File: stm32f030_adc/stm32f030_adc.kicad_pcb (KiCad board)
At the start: 2 copper layers, 41 parts, among them Q1 BC337, U1 STM32F103C6Tx, U2 AMS1117-3.3, X1 USB_B_Micro, Y2 8 MHz

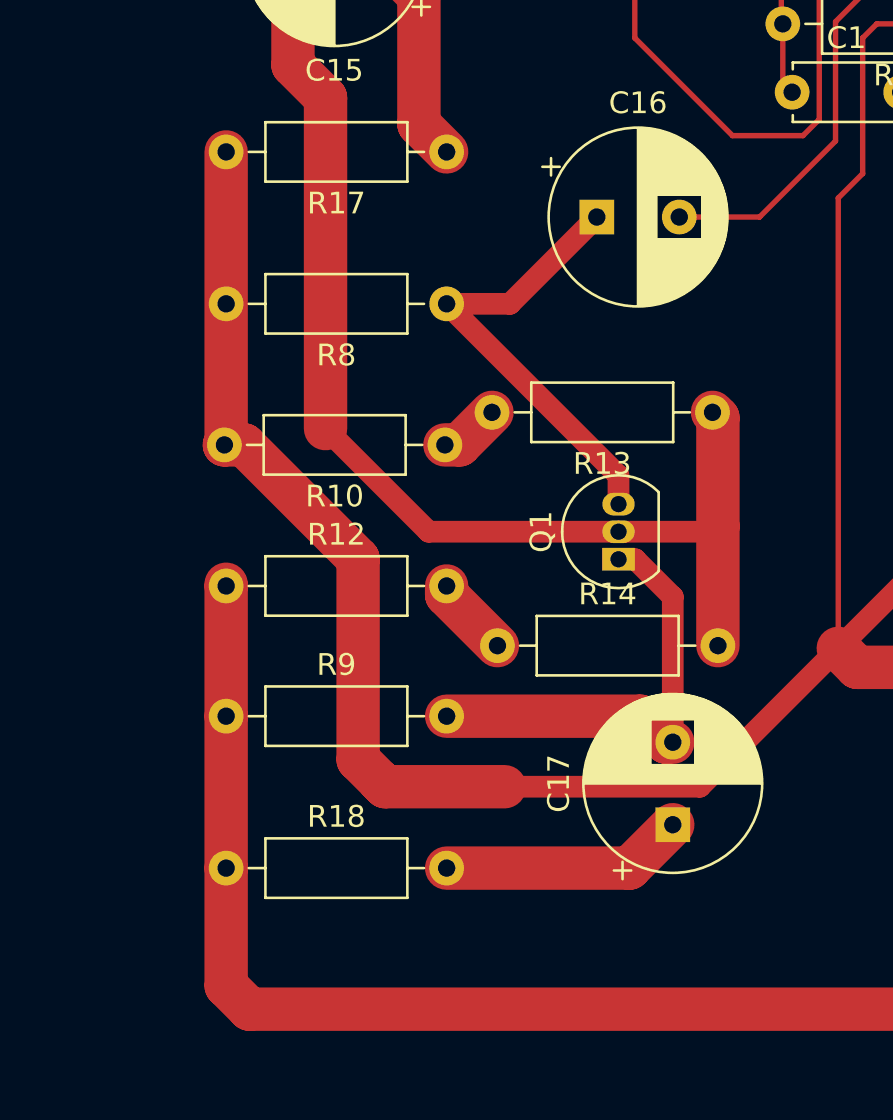
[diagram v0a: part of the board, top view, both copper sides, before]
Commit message: Extensibility: more jumpers, intermediate result, the layout is not complete
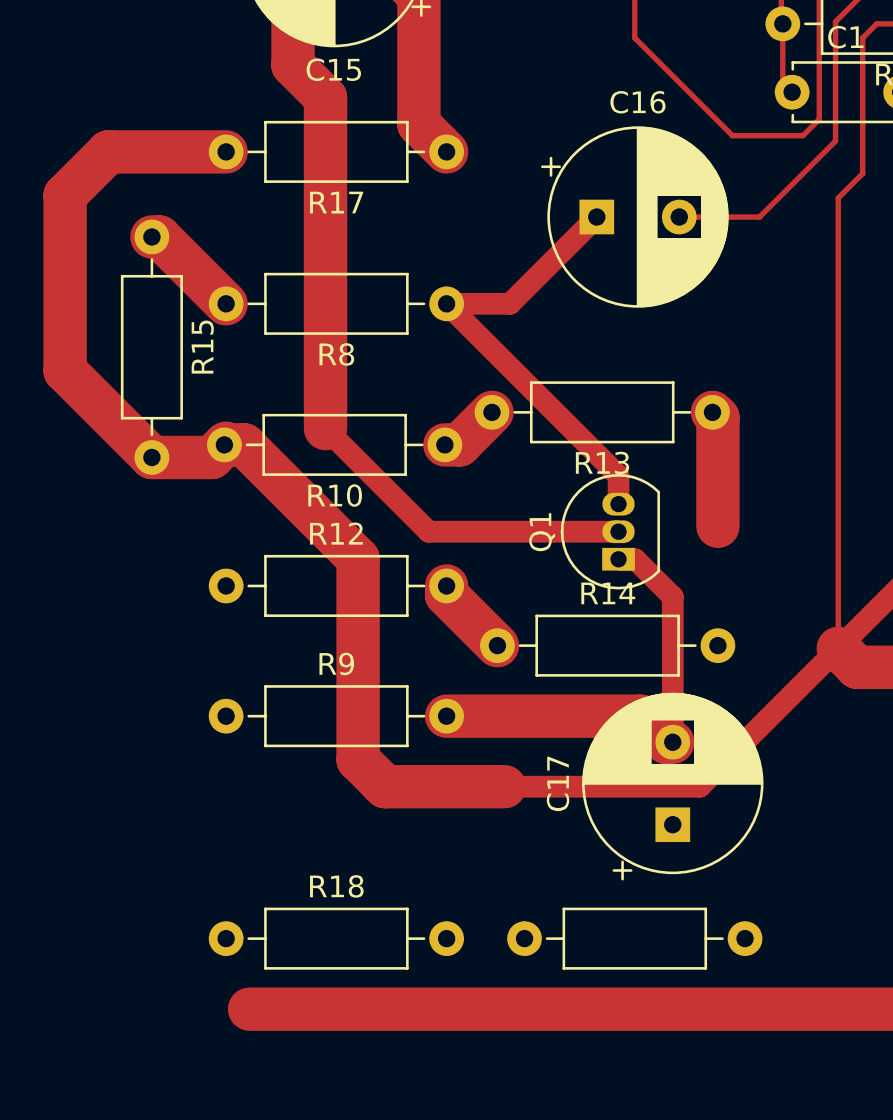
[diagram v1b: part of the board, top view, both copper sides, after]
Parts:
- added R15: 0, Resistor_THT:R_Axial_DIN0207_L6.3mm_D2.5mm_P10.16mm_Horizontal, F.Cu at (110.8, 109.9)
- added R16: 0, Resistor_THT:R_Axial_DIN0207_L6.3mm_D2.5mm_P10.16mm_Horizontal, F.Cu at (127.9, 142.2)
- moved R18 3.25 mm to (114.2, 142.2)
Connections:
- R18 pad 2: Net-(C17-Pad1) -> Net-(R16-Pad1)
- R8 pad 2: +3V3 -> Net-(R15-Pad1)
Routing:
- net GNDREF: track 421.7 -> 401.6 mm
- net +3V3: track 232.9 -> 245.1 mm
- net Net-(C17-Pad1): track 11.2 -> 0.00 mm
- net Net-(Q1-B): track 53.4 -> 43.2 mm
- net Net-(R15-Pad1): track 0.00 -> 4.70 mm

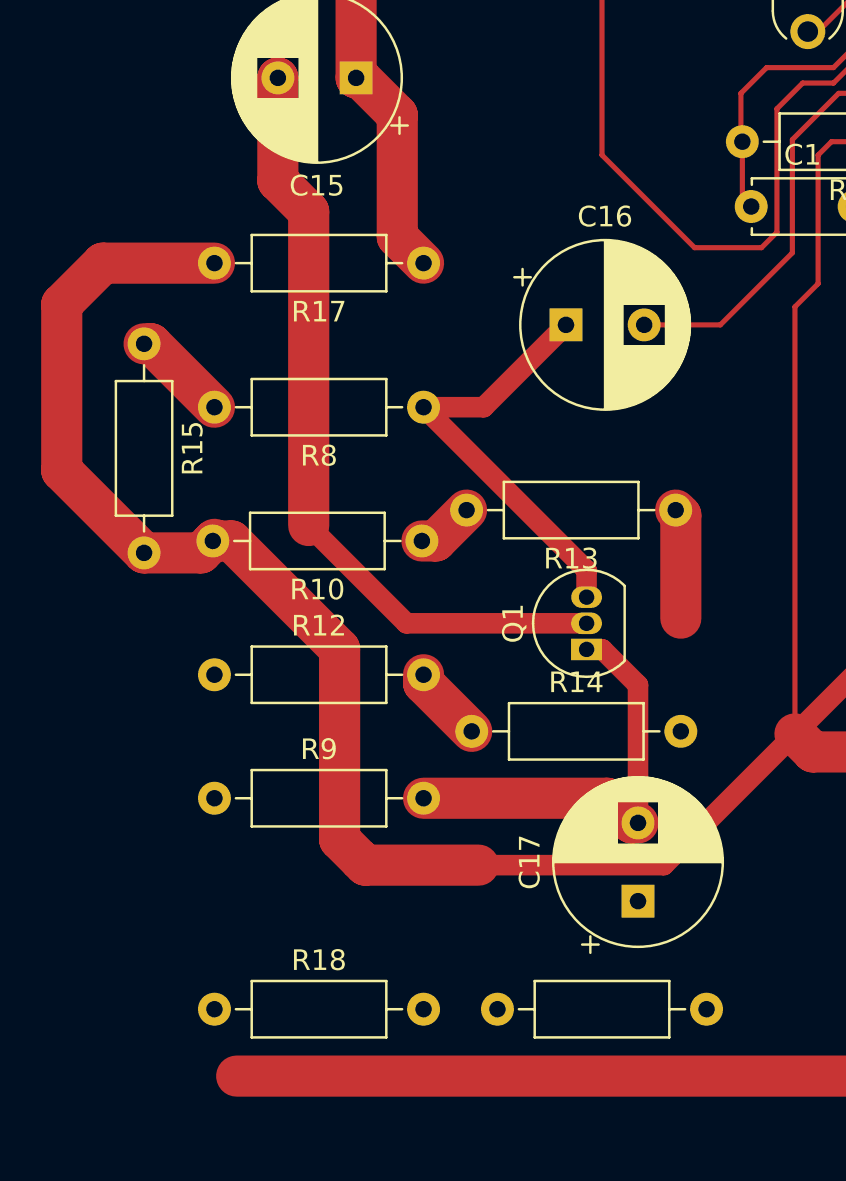
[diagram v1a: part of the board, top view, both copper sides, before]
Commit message: Esthetics: jumpers
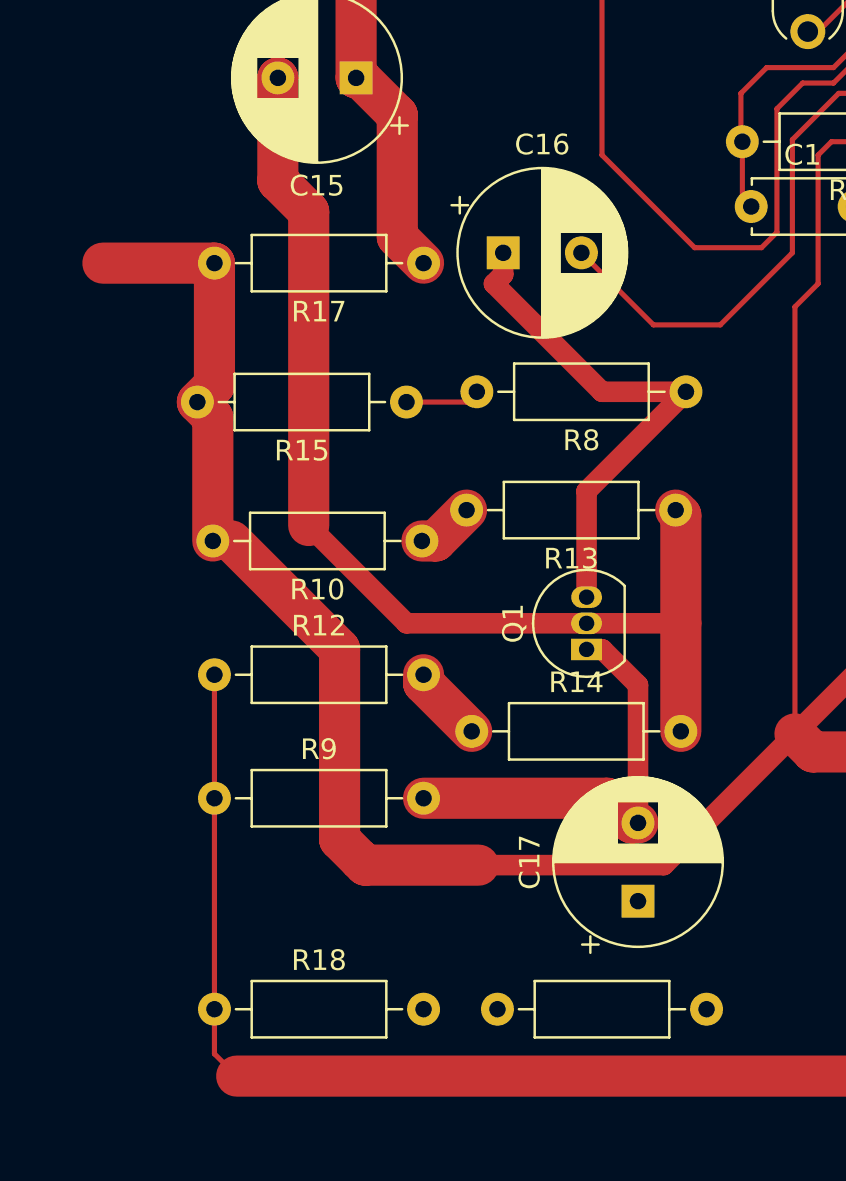
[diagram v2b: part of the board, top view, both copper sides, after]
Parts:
- moved R15 13.1 mm to (123.5, 112.8), turned to 180 degrees
- moved R8 12.8 mm to (137.1, 112.2)
- moved C16 4.64 mm to (128.2, 105.5)
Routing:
- net GNDREF: track 401.6 -> 421.6 mm
- net Net-(Q1-B): track 43.2 -> 53.3 mm
- net +3V3: track 245.1 -> 238.1 mm
- net /Electret AMP/MIC_AMP_OUT: track 25.1 -> 29.6 mm
- net Net-(Q1-C): track 21.1 -> 25.2 mm
- net Net-(R15-Pad1): track 4.70 -> 3.63 mm

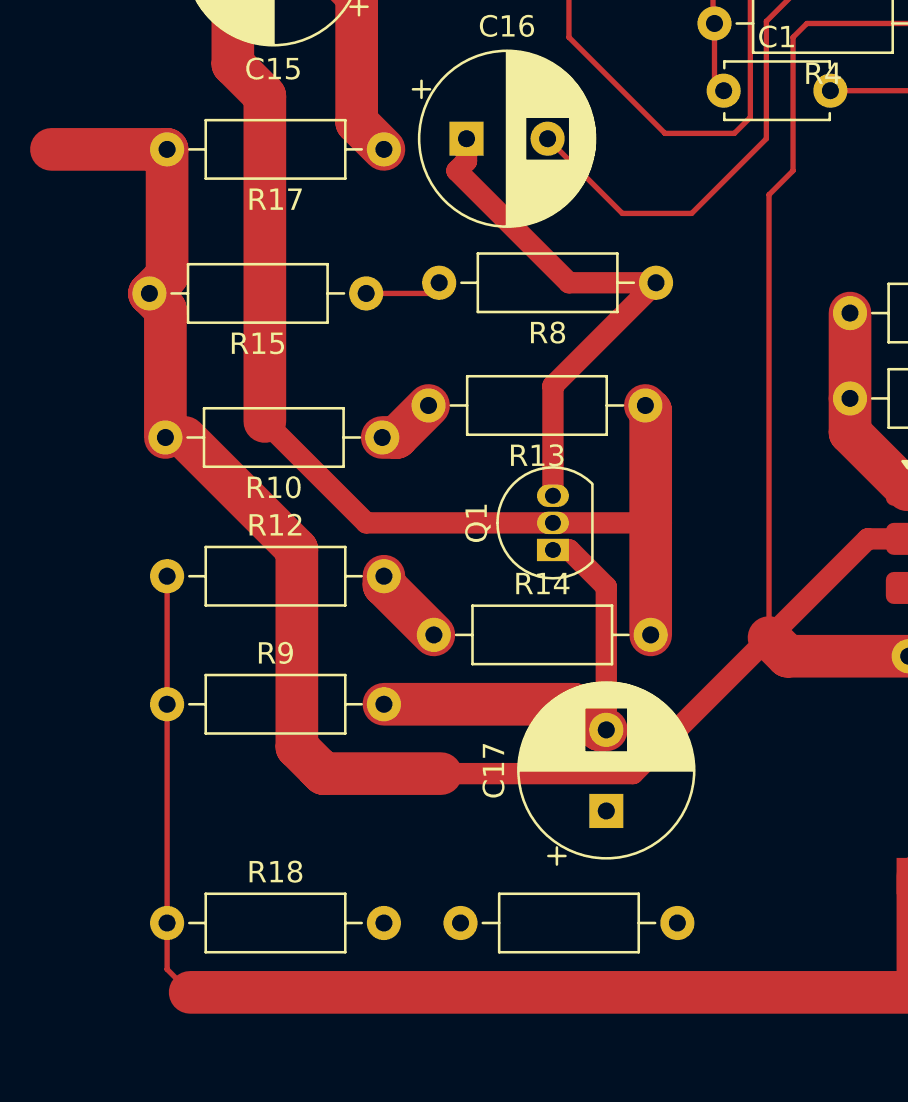
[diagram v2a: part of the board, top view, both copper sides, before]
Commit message: Esthetics: placement
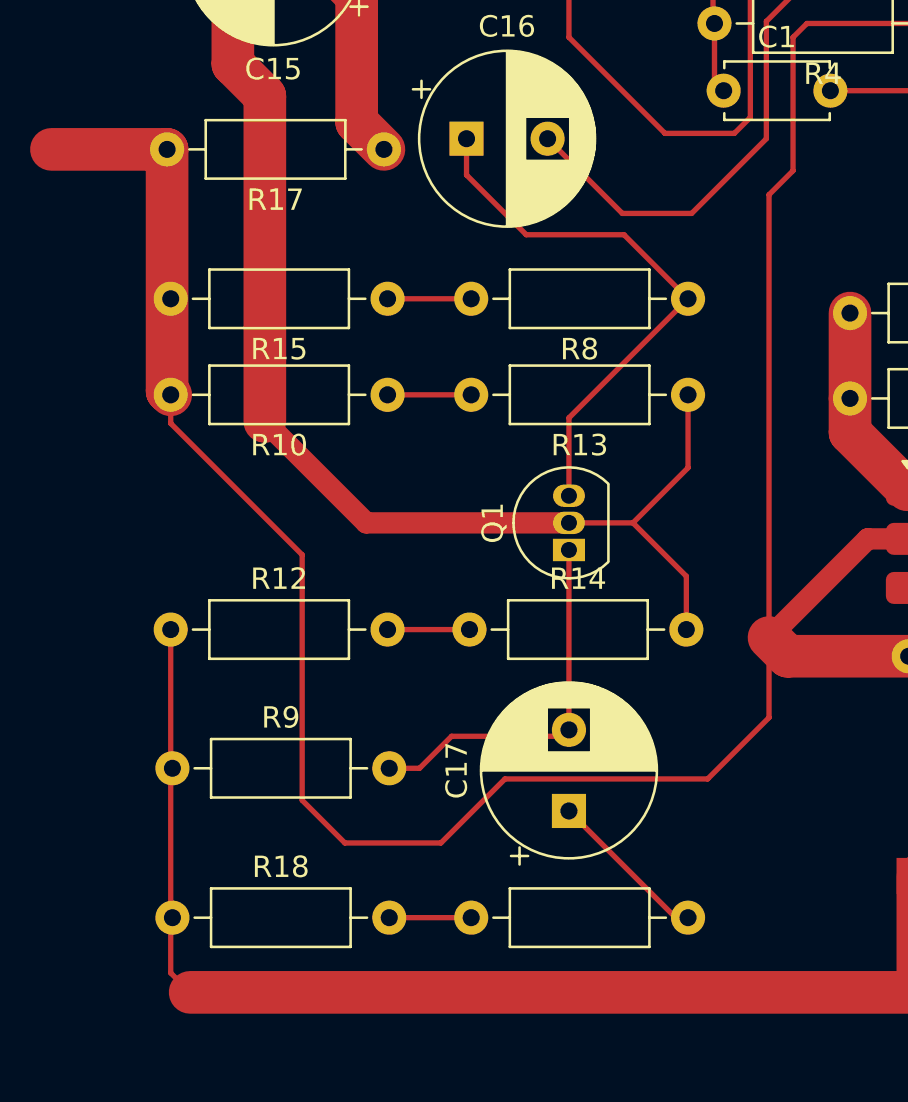
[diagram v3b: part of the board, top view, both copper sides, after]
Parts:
- moved R9 3.01 mm to (114.4, 135.0)
- moved R12 2.51 mm to (114.3, 128.5)
- moved R13 2.06 mm to (138.6, 117.5)
- moved R10 2.02 mm to (124.5, 117.5)
- moved C17 1.75 mm to (133.0, 137.0)
- moved R14 1.69 mm to (128.3, 128.5)
- moved R8 1.68 mm to (138.6, 113.0)
- moved R15 1.03 mm to (124.5, 113.0)
- moved Q1 0.75 mm to (133.0, 124.8)
- moved R16 0.56 mm to (128.4, 142.0)
- moved R18 0.35 mm to (114.4, 142.0)
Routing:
- net Net-(C17-Pad1): track 0.00 -> 7.65 mm
- net +3V3: track 238.1 -> 244.0 mm
- net Net-(R16-Pad1): track 0.00 -> 3.84 mm
- net Net-(Q1-E): track 20.8 -> 17.6 mm
- net GNDREF: track 421.6 -> 419.0 mm
- net Net-(Q1-B): track 53.3 -> 54.7 mm
- net Net-(R10-Pad1): track 2.79 -> 3.92 mm
- net Net-(Q1-C): track 25.2 -> 26.0 mm

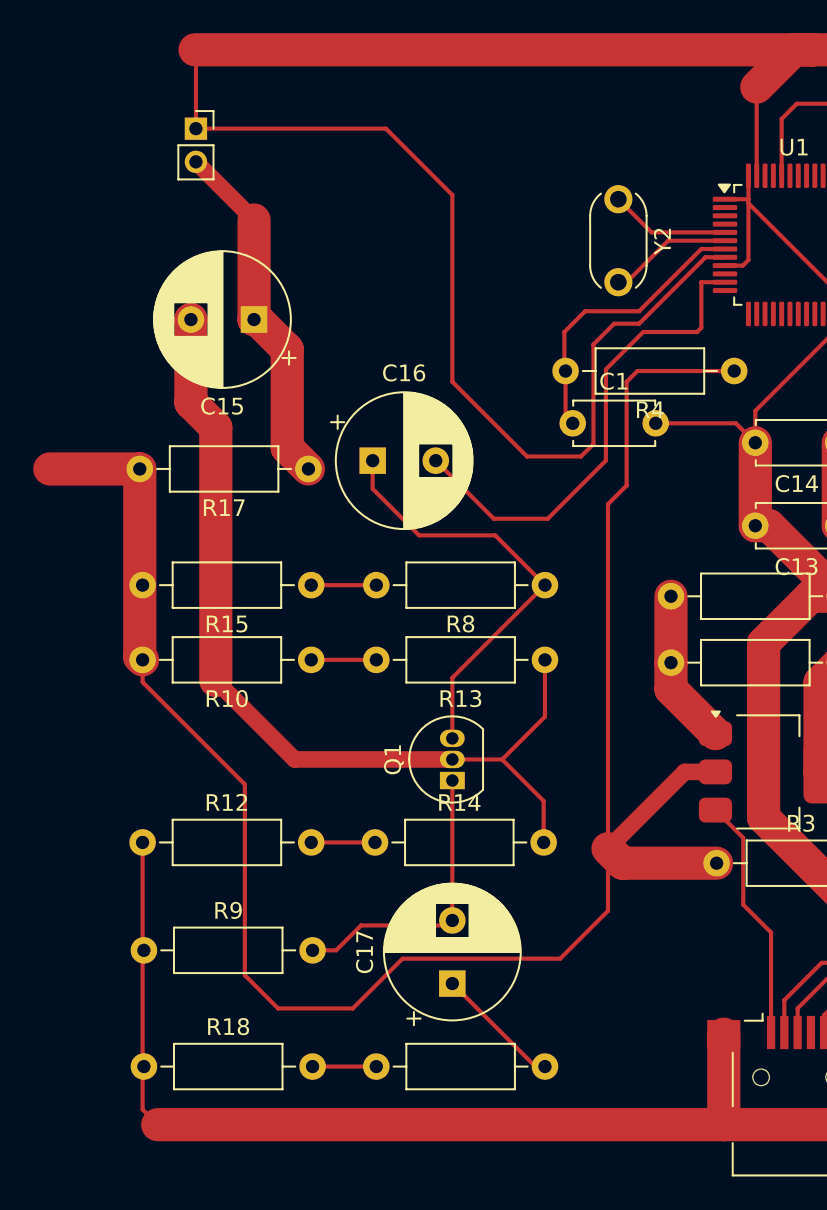
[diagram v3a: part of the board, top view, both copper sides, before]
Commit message: Layout: done w/ placement, and extensions
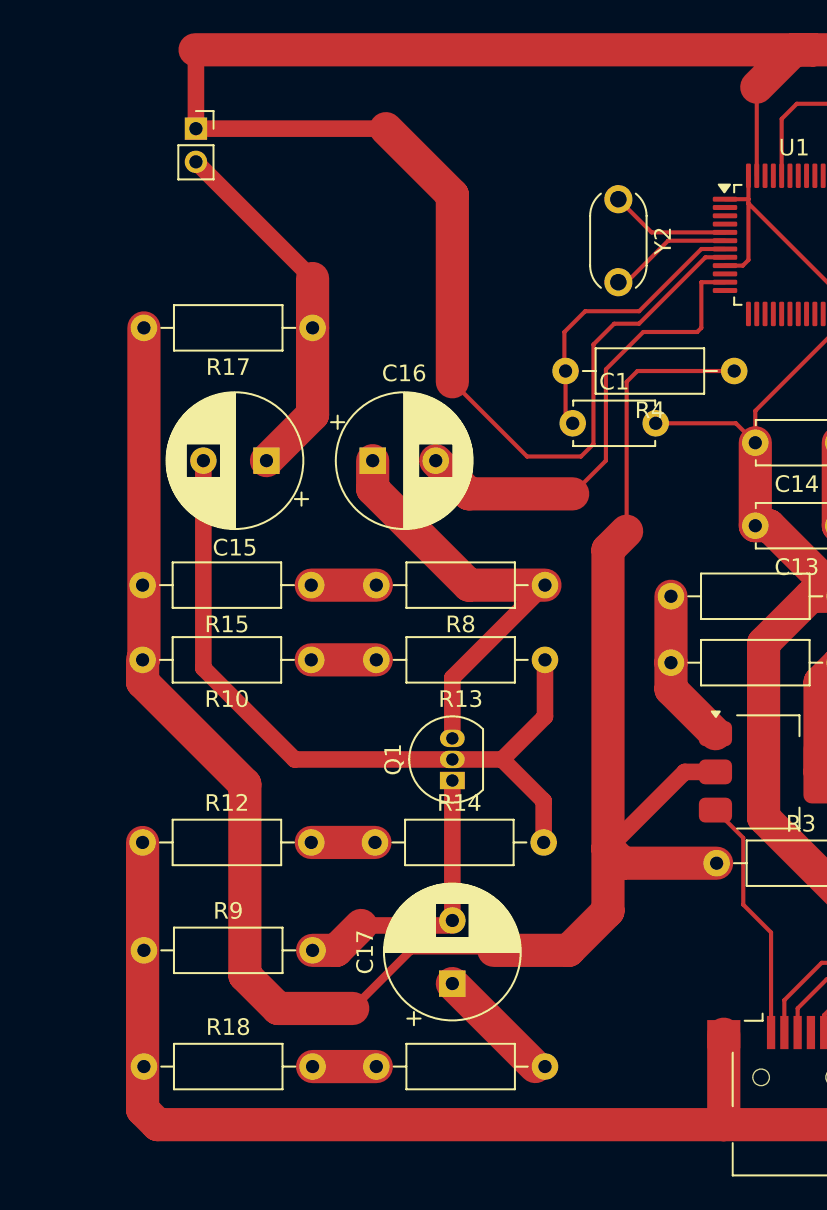
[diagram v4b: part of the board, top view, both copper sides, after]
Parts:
- moved C15 8.53 mm to (121.8, 105.5)
- moved R17 8.50 mm to (124.6, 97.5)
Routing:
- net Net-(Q1-B): track 54.7 -> 45.9 mm
- net +3V3: track 244.0 -> 246.9 mm
- net /Electret AMP/MIC_AMP_OUT: track 29.6 -> 28.4 mm
- net Net-(MK1-+): track 21.4 -> 22.1 mm
- net Net-(C17-Pad1): track 7.65 -> 7.07 mm

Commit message: Dimensions: narrower
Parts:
- moved C15 3.42 mm to (125.2, 105.5)
- moved MK1 3.42 mm to (121.0, 85.5)
- moved R10 3.42 mm to (127.9, 117.5)
- moved R12 3.42 mm to (117.8, 128.5)
- moved R15 3.42 mm to (127.9, 113.0)
- moved R17 3.42 mm to (128.0, 97.5)
- moved R18 3.42 mm to (117.8, 142.0)
- moved R9 3.42 mm to (117.8, 135.0)
- moved C16 2.50 mm to (130.7, 105.5)
- moved C17 2.50 mm to (135.5, 137.0)
- moved Q1 2.50 mm to (135.5, 124.8)
- moved R13 2.50 mm to (141.1, 117.5)
- moved R14 2.50 mm to (130.8, 128.5)
- moved R16 2.50 mm to (130.9, 142.0)
- moved R8 2.50 mm to (141.1, 113.0)
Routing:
- net GNDREF: track 419.0 -> 408.0 mm
- net +3V3: track 246.9 -> 241.9 mm
- net /Electret AMP/MIC_AMP_OUT: track 28.4 -> 25.9 mm
- net Net-(R16-Pad1): track 3.84 -> 2.92 mm
- net Net-(R15-Pad1): track 3.92 -> 3.00 mm
- net Net-(R12-Pad2): track 3.84 -> 2.92 mm
- net Net-(R10-Pad1): track 3.92 -> 3.00 mm
- net Net-(Q1-E): track 17.6 -> 16.7 mm
- net Net-(Q1-B): track 45.9 -> 45.0 mm
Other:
- board outline added: 61.5 x 68.8 mm

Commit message: Narrowed
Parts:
- added R19: 0, Resistor_THT:R_Axial_DIN0207_L6.3mm_D2.5mm_P10.16mm_Horizontal, F.Cu at (141.1, 145.5)
- added R20: 0, Resistor_THT:R_Axial_DIN0207_L6.3mm_D2.5mm_P10.16mm_Horizontal, F.Cu at (138.5, 107.0)
- added R21: 0, Resistor_THT:R_Axial_DIN0207_L6.3mm_D2.5mm_P10.16mm_Horizontal, F.Cu at (140.9, 83.7)
- added R22: 0, Resistor_THT:R_Axial_DIN0207_L6.3mm_D2.5mm_P10.16mm_Horizontal, F.Cu at (140.7, 71.5)
- moved MK1 45.1 mm to (162.5, 68.0), turned to -90 degrees
- moved C15 39.7 mm to (151.7, 76.0)
- moved C16 39.7 mm to (157.2, 76.0)
- moved R17 39.7 mm to (154.5, 68.0)
- moved R15 37.6 mm to (130.6, 75.5), turned to 0 degrees
- moved R8 33.5 mm to (141.0, 79.5)
- moved R10 30.4 mm to (130.8, 87.2), turned to 0 degrees
- moved R12 27.1 mm to (138.5, 111.0), turned to 180 degrees
- moved R13 26.9 mm to (141.0, 90.6)
- moved Q1 23.0 mm to (130.9, 102.3)
- moved R18 14.8 mm to (130.9, 149.0)
- moved R9 14.7 mm to (129.4, 126.0)
- moved R14 13.7 mm to (128.4, 115.0)
- moved C2 3.79 mm to (166.5, 88.9)
- moved C7 3.79 mm to (166.5, 109.2)
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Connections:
- R10 pad 2: +3V3 -> Net-(R10-Pad2)
- R14 pad 2: Net-(Q1-B) -> Net-(R14-Pad2)
- R15 pad 2: +3V3 -> Net-(R15-Pad2)
- R18 pad 2: Net-(R16-Pad1) -> Net-(R18-Pad2)
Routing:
- net /Electret AMP/MIC_AMP_OUT: track 25.9 -> 94.5 mm
- net +3V3: track 241.9 -> 293.7 mm
- net Net-(Q1-C): track 26.0 -> 57.5 mm
- net Net-(Q1-B): track 45.0 -> 69.0 mm
- net Net-(Q1-E): track 16.7 -> 36.6 mm
- net GNDREF: track 408.0 -> 393.3 mm
- net Net-(R14-Pad2): track 0.00 -> 9.74 mm
- net Net-(MK1-+): track 22.1 -> 15.2 mm
- net Net-(X1-D+): track 21.6 -> 15.5 mm
- net Net-(R15-Pad2): track 0.00 -> 4.03 mm
- net Net-(U1-PD1): track 7.46 -> 3.74 mm
- net Net-(R10-Pad2): track 0.00 -> 3.53 mm
- net Net-(U1-BOOT0): track 16.1 -> 12.6 mm
- net Net-(R18-Pad2): track 0.00 -> 3.50 mm
- net /Power and MCU/USB_D-: track 39.6 -> 37.7 mm
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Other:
- board outline removed

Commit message: Ref: dead line
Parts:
- moved X1 10.6 mm to (148.2, 151.7)
- moved TP2 1.00 mm to (158.8, 86.0)
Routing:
- net GNDREF: track 393.3 -> 367.2 mm
- net Net-(Q1-B): track 69.0 -> 47.8 mm
- net Net-(X1-D+): track 15.5 -> 26.9 mm
- net Net-(X1-D-): track 12.8 -> 24.2 mm
- net 5V_USB: track 14.8 -> 25.2 mm
- net /Power and MCU/SWD_CLK: track 5.36 -> 4.36 mm
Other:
- board outline added: 50 x 93.5 mm
